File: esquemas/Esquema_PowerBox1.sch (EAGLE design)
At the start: 22 parts

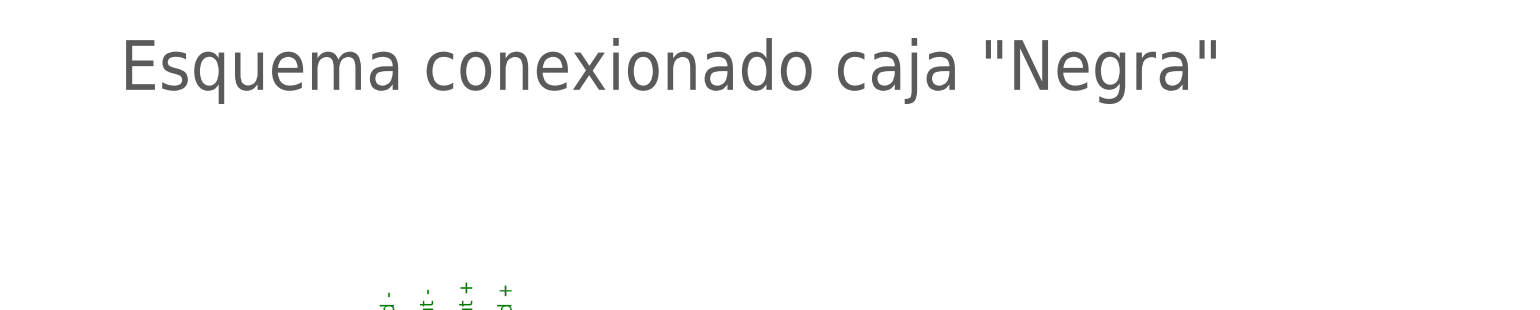
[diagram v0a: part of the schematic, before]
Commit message: Modificación
Modificación del texto en PowerBox1, adición del programador en Curtis y
redistribución de algunos elementos
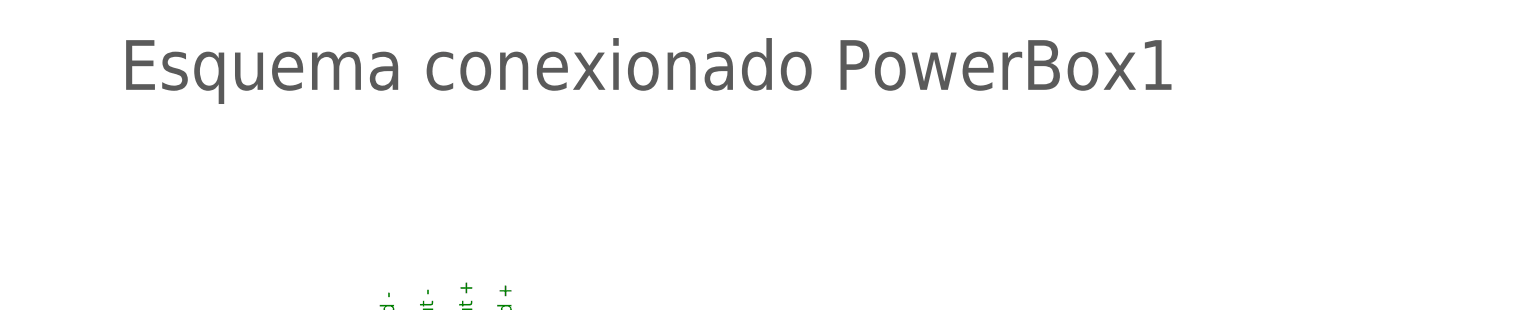
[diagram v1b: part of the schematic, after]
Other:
- note added: "Esquema conexionado PowerBox1"
- note removed: "Esquema conexionado caja "Negra""
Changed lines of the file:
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@@
 <setting verticaltext="up"/>
 </settings>
-<grid distance="0.1" unitdist="inch" unit="mm" style="lines" multiple="1" display="yes" altdistance="0.01" altunitdist="inch" altunit="mm"/>
+<grid distance="0.1" unitdist="inch" unit="inch" style="lines" multiple="1" display="no" altdistance="0.01" altunitdist="inch" altunit="inch"/>
 <layers>
 <layer number="1" name="Top" color="4" fill="1" visible="no" active="no"/>
@@
 <text x="-7.62" y="60.96" size="1.778" layer="91">I. General</text>
 <text x="119.38" y="48.26" size="1.778" layer="91">A DC-DC 12v (1)</text>
-<text x="-20.32" y="134.62" size="6.4516" layer="92">Esquema conexionado caja "Negra"</text>
+<text x="-20.32" y="134.62" size="6.4516" layer="92">Esquema conexionado PowerBox1</text>
 </plain>
 <instances>

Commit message: Actualización de la documentación
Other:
- note added: "A ORDENADOR"
- note removed: "A DC-DC 12v (1)"
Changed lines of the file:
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@@
 <text x="30.48" y="101.6" size="1.778" layer="91" rot="R90">Load +</text>
 <text x="-7.62" y="60.96" size="1.778" layer="91">I. General</text>
-<text x="119.38" y="48.26" size="1.778" layer="91">A DC-DC 12v (1)</text>
+<text x="119.38" y="48.26" size="1.778" layer="91">A ORDENADOR</text>
 <text x="-20.32" y="134.62" size="6.4516" layer="92">Esquema conexionado PowerBox1</text>
 </plain>
